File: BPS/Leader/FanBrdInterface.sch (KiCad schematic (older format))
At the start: 15 parts, among them J12 FanBrdConn, U14 SI8261ABC-IS, U15 SI8261ABC-IS, U16 SI8261ABC-IS, U17 SI8261ABC-IS

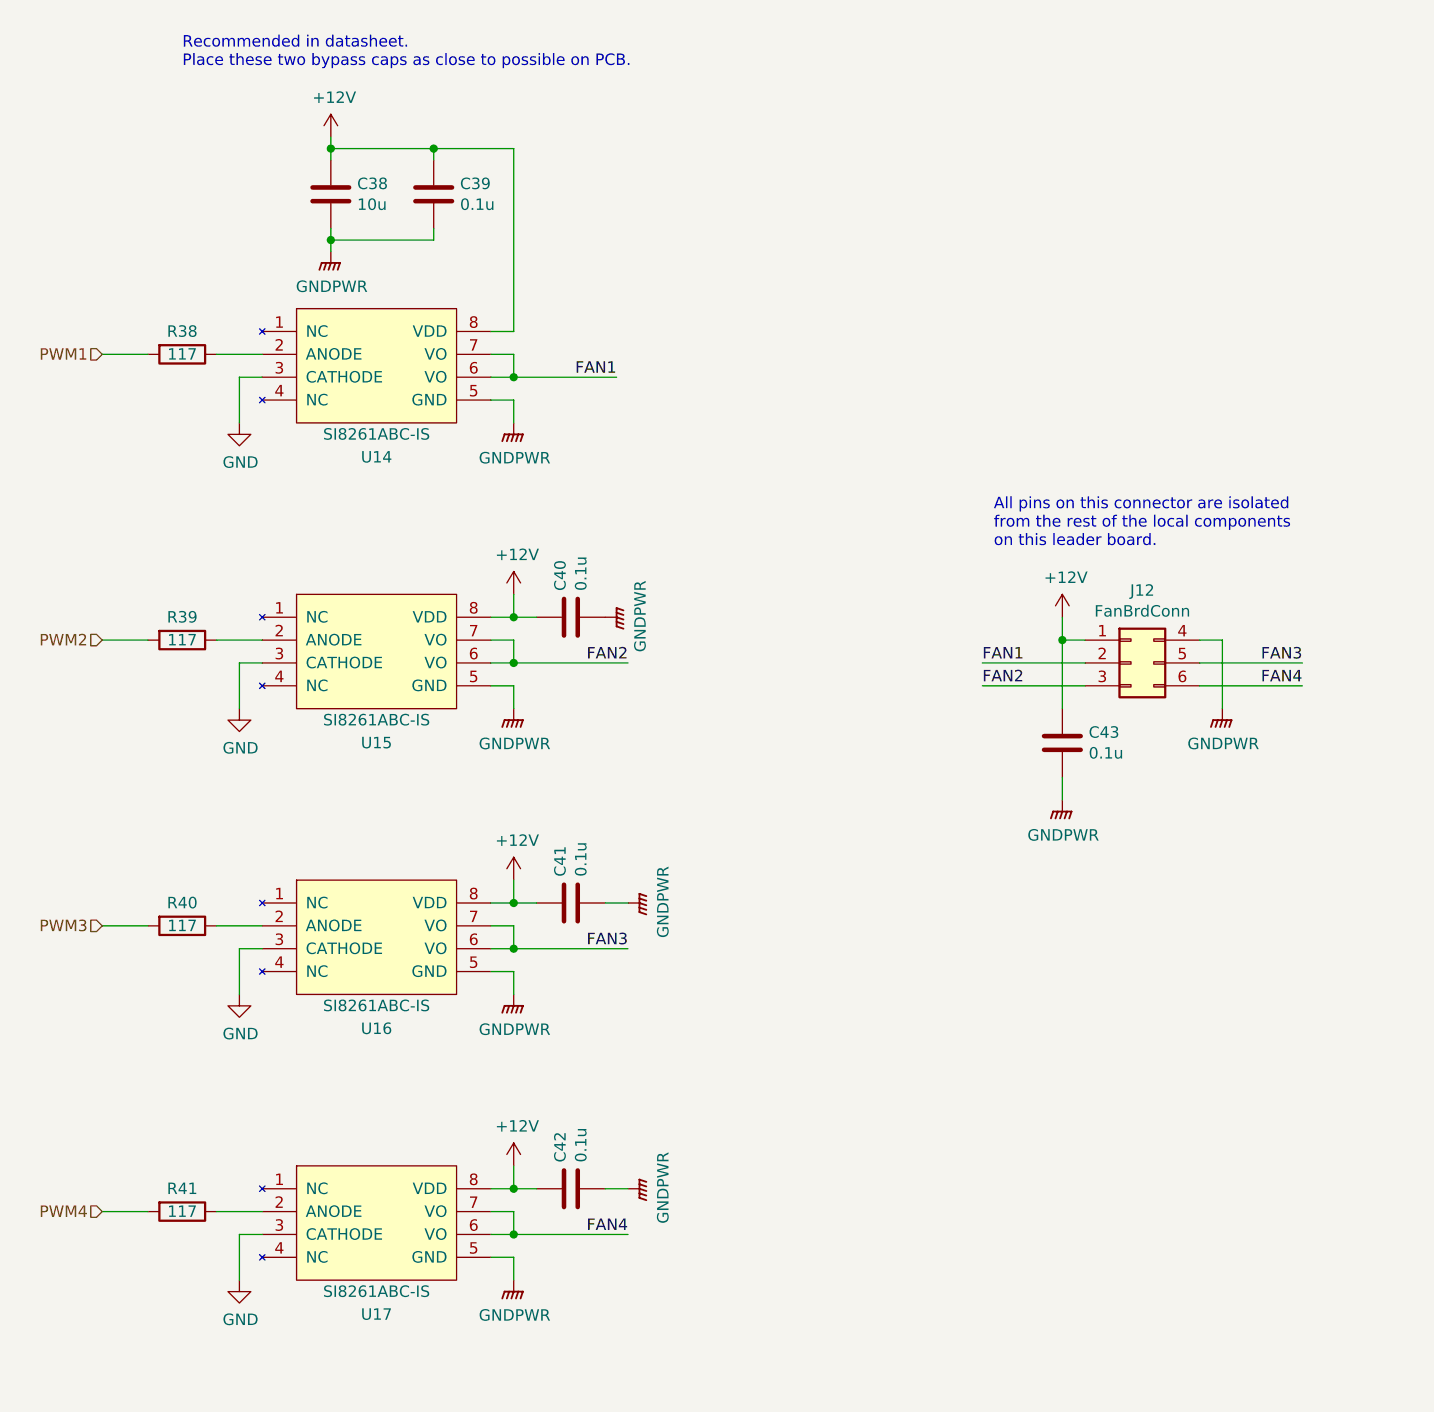
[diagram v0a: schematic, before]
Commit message: Places most components of leader board in their respective locations with nothing traced
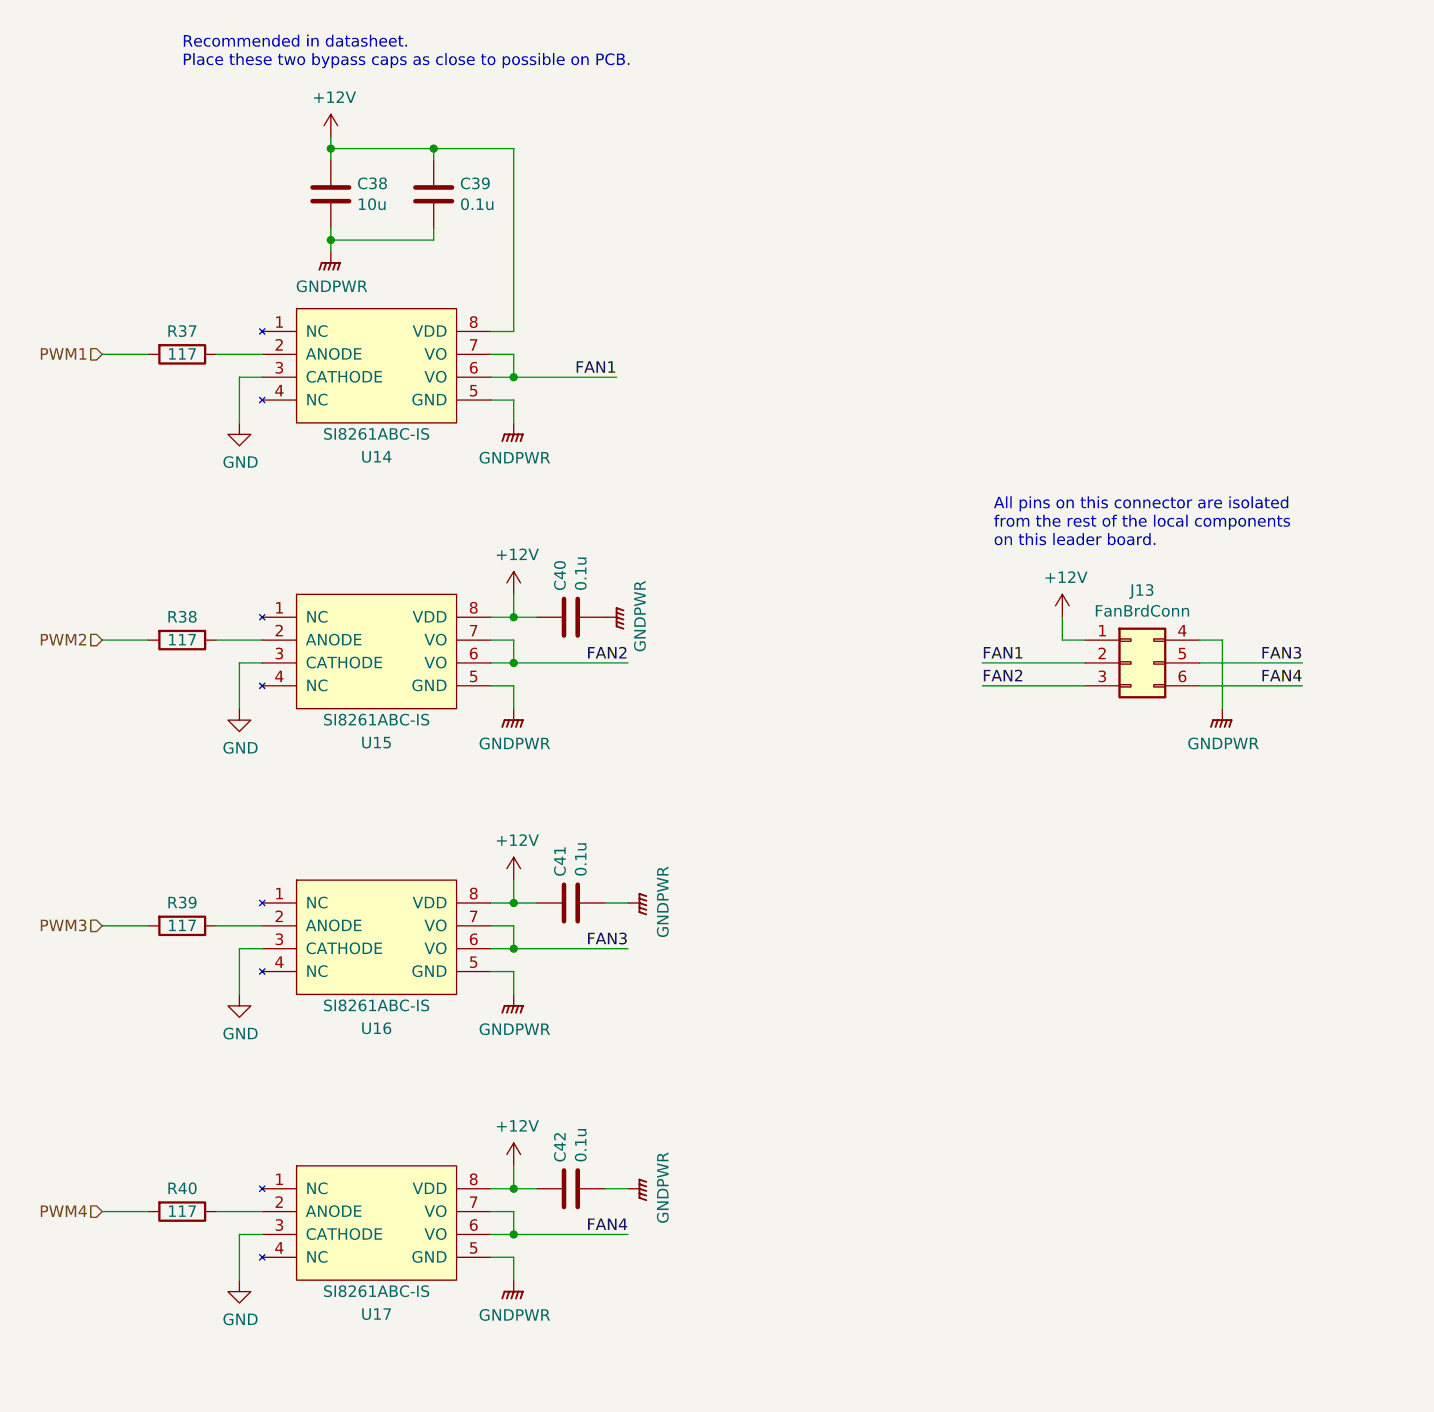
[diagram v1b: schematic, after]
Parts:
- removed C43: 0.1u, Capacitor_SMD:C_0805_2012Metric, symbol Device:C
- renumbered J12 to J13, R38 to R37, R39 to R38, R40 to R39, R41 to R40
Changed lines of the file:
@@
 $EndComp
 $Comp
-L Device:R R38
+L Device:R R37
 U 1 1 5F14C350
 P 3450 2700
-F 0 "R38" V 3350 2700 50  0000 C CNN
+F 0 "R37" V 3350 2700 50  0000 C CNN
 F 1 "117" V 3450 2700 50  0000 C CNN
 F 2 "Resistor_SMD:R_0805_2012Metric" V 3380 2700 50  0001 C CNN
@@
 	3100 2700 3300 2700
 $Comp
-L Connector_Generic:Conn_02x03_Top_Bottom J12
+L Connector_Generic:Conn_02x03_Top_Bottom J13
 U 1 1 5F14E9E0
 P 7600 4050
-F 0 "J12" H 7650 4367 50  0000 C CNN
+F 0 "J13" H 7650 4367 50  0000 C CNN
 F 1 "FanBrdConn" H 7650 4276 50  0000 C CNN
 F 2 "Connector_Molex:Molex_Micro-Fit_3.0_43045-0612_2x03_P3.00mm_Vertical" H 7600 4050 50  0001 C CNN
@@
 $EndComp
 $Comp
-L Device:R R39
+L Device:R R38
 U 1 1 5F15320D
 P 3450 3950
-F 0 "R39" V 3350 3950 50  0000 C CNN
+F 0 "R38" V 3350 3950 50  0000 C CNN
 F 1 "117" V 3450 3950 50  0000 C CNN
 F 2 "Resistor_SMD:R_0805_2012Metric" V 3380 3950 50  0001 C CNN
@@
 $EndComp
 $Comp
-L Device:R R40
+L Device:R R39
 U 1 1 5F155481
 P 3450 5200
-F 0 "R40" V 3350 5200 50  0000 C CNN
+F 0 "R39" V 3350 5200 50  0000 C CNN
 F 1 "117" V 3450 5200 50  0000 C CNN
 F 2 "Resistor_SMD:R_0805_2012Metric" V 3380 5200 50  0001 C CNN
@@
 P 8000 4250
 AR Path="/5C38C674/5F15A290" Ref="#PWR?"  Part="1"
-AR Path="/5F145F02/5F15A290" Ref="#PWR099"  Part="1"
-F 0 "#PWR099" H 8000 4050 50  0001 C CNN
+AR Path="/5F145F02/5F15A290" Ref="#PWR098"  Part="1"
+F 0 "#PWR098" H 8000 4050 50  0001 C CNN
 F 1 "GNDPWR" H 8004 4096 50  0000 C CNN
 F 2 "" H 8000 4200 50  0001 C CNN
@@
 $EndComp
 $Comp
-L Device:R R41
+L Device:R R40
 U 1 1 5F16451F
 P 3450 6450
-F 0 "R41" V 3350 6450 50  0000 C CNN
+F 0 "R40" V 3350 6450 50  0000 C CNN
 F 1 "117" V 3450 6450 50  0000 C CNN
 F 2 "Resistor_SMD:R_0805_2012Metric" V 3380 6450 50  0001 C CNN
@@
 	4900 3750 4900 3850
 $Comp
-L Device:C C43
-U 1 1 5F1A07F9
-P 7300 4400
-F 0 "C43" H 7415 4446 50  0000 L CNN
-F 1 "0.1u" H 7415 4355 50  0000 L CNN
-F 2 "Capacitor_SMD:C_0805_2012Metric" H 7338 4250 50  0001 C CNN
-F 3 "~" H 7300 4400 50  0001 C CNN
-	1    7300 4400
-	1    0    0    -1
-$EndComp
-Wire Wire Line
-	7300 4250 7300 3950
-Connection ~ 7300 3950
-$Comp
-L power:GNDPWR #PWR?
-U 1 1 5F1A1FAF
-P 7300 4650
-AR Path="/5C38C674/5F1A1FAF" Ref="#PWR?"  Part="1"
-AR Path="/5F145F02/5F1A1FAF" Ref="#PWR098"  Part="1"
-F 0 "#PWR098" H 7300 4450 50  0001 C CNN
-F 1 "GNDPWR" H 7304 4496 50  0000 C CNN
-F 2 "" H 7300 4600 50  0001 C CNN
-F 3 "" H 7300 4600 50  0001 C CNN
-	1    7300 4650
-	1    0    0    -1
-$EndComp
-Wire Wire Line
-	7300 4650 7300 4550
-$Comp
 L Device:C C?

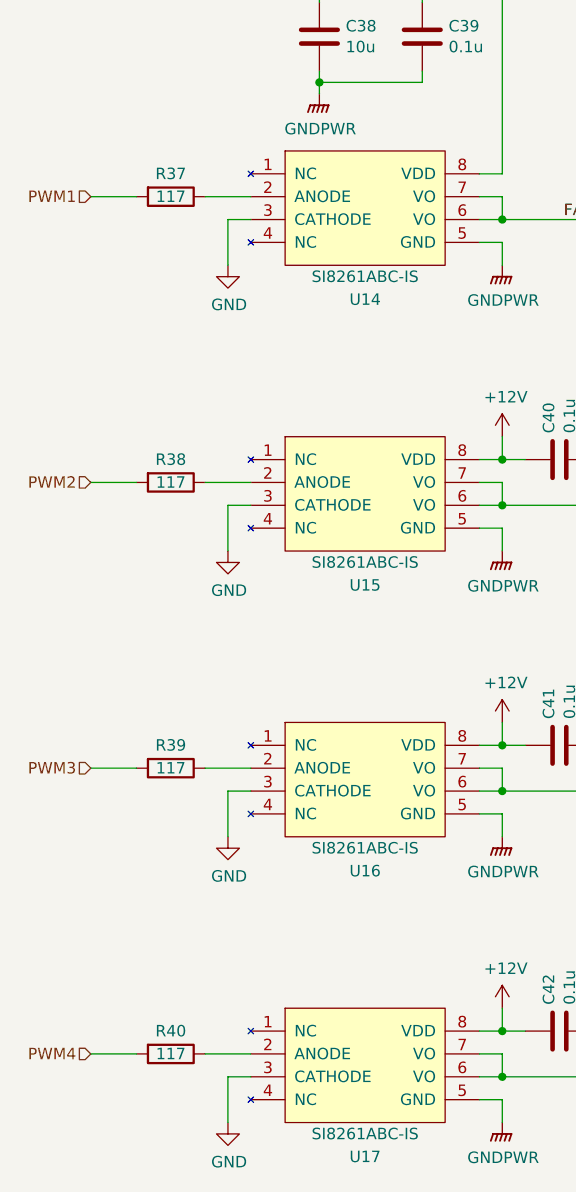
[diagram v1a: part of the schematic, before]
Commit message: Adds power planes
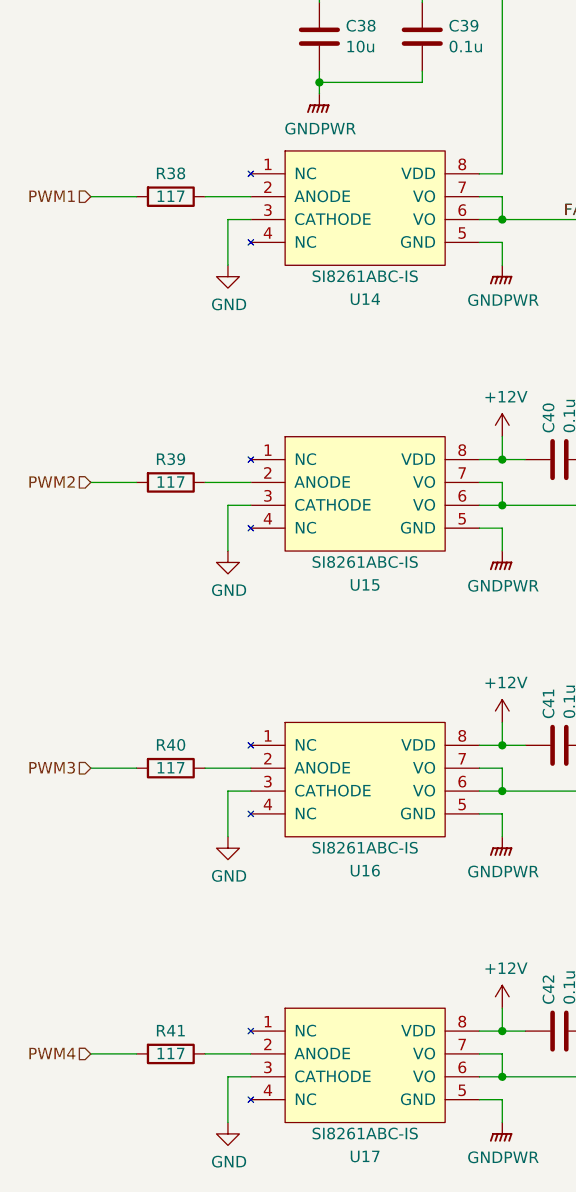
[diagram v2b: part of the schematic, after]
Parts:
- renumbered R37 to R38, R38 to R39, R39 to R40, R40 to R41
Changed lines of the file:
@@
 $EndComp
 $Comp
-L Device:R R37
+L Device:R R38
 U 1 1 5F14C350
 P 3450 2700
-F 0 "R37" V 3350 2700 50  0000 C CNN
+F 0 "R38" V 3350 2700 50  0000 C CNN
 F 1 "117" V 3450 2700 50  0000 C CNN
 F 2 "Resistor_SMD:R_0805_2012Metric" V 3380 2700 50  0001 C CNN
@@
 $EndComp
 $Comp
-L Device:R R38
+L Device:R R39
 U 1 1 5F15320D
 P 3450 3950
-F 0 "R38" V 3350 3950 50  0000 C CNN
+F 0 "R39" V 3350 3950 50  0000 C CNN
 F 1 "117" V 3450 3950 50  0000 C CNN
 F 2 "Resistor_SMD:R_0805_2012Metric" V 3380 3950 50  0001 C CNN
@@
 $EndComp
 $Comp
-L Device:R R39
+L Device:R R40
 U 1 1 5F155481
 P 3450 5200
-F 0 "R39" V 3350 5200 50  0000 C CNN
+F 0 "R40" V 3350 5200 50  0000 C CNN
 F 1 "117" V 3450 5200 50  0000 C CNN
 F 2 "Resistor_SMD:R_0805_2012Metric" V 3380 5200 50  0001 C CNN
@@
 $EndComp
 $Comp
-L Device:R R40
+L Device:R R41
 U 1 1 5F16451F
 P 3450 6450
-F 0 "R40" V 3350 6450 50  0000 C CNN
+F 0 "R41" V 3350 6450 50  0000 C CNN
 F 1 "117" V 3450 6450 50  0000 C CNN
 F 2 "Resistor_SMD:R_0805_2012Metric" V 3380 6450 50  0001 C CNN
